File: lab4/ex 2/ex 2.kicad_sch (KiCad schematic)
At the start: 10 parts, among them J1 Conn_01x02_Male, U1 NE555D

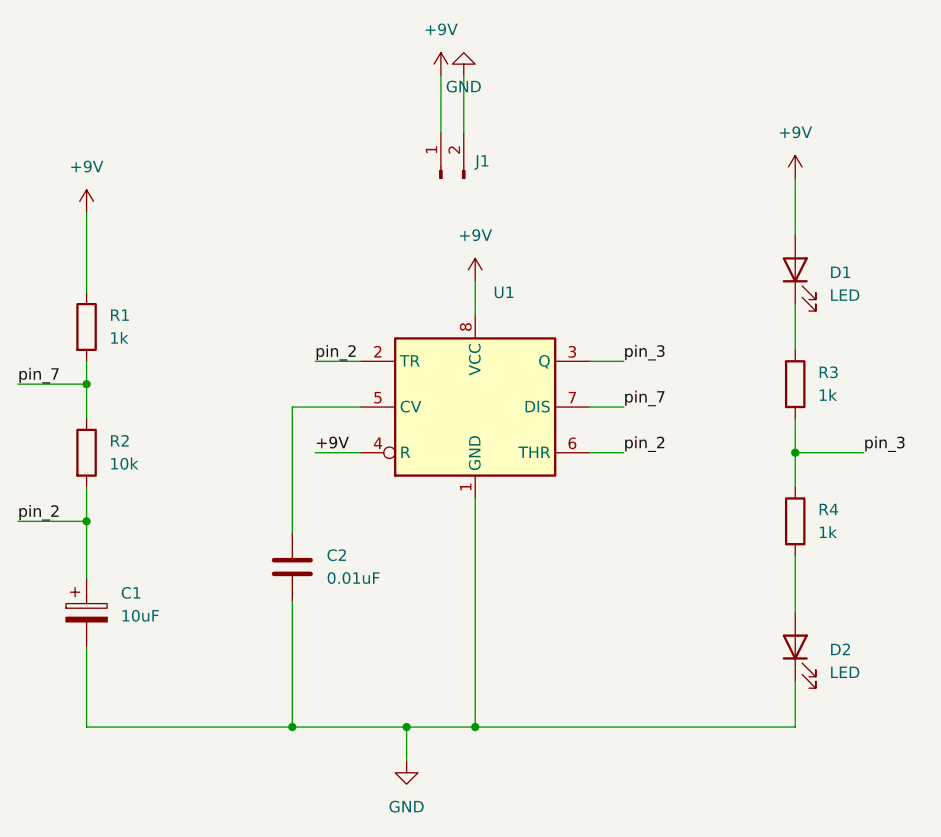
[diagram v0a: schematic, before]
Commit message: Updated schematics to include footprints and created a pcb layout
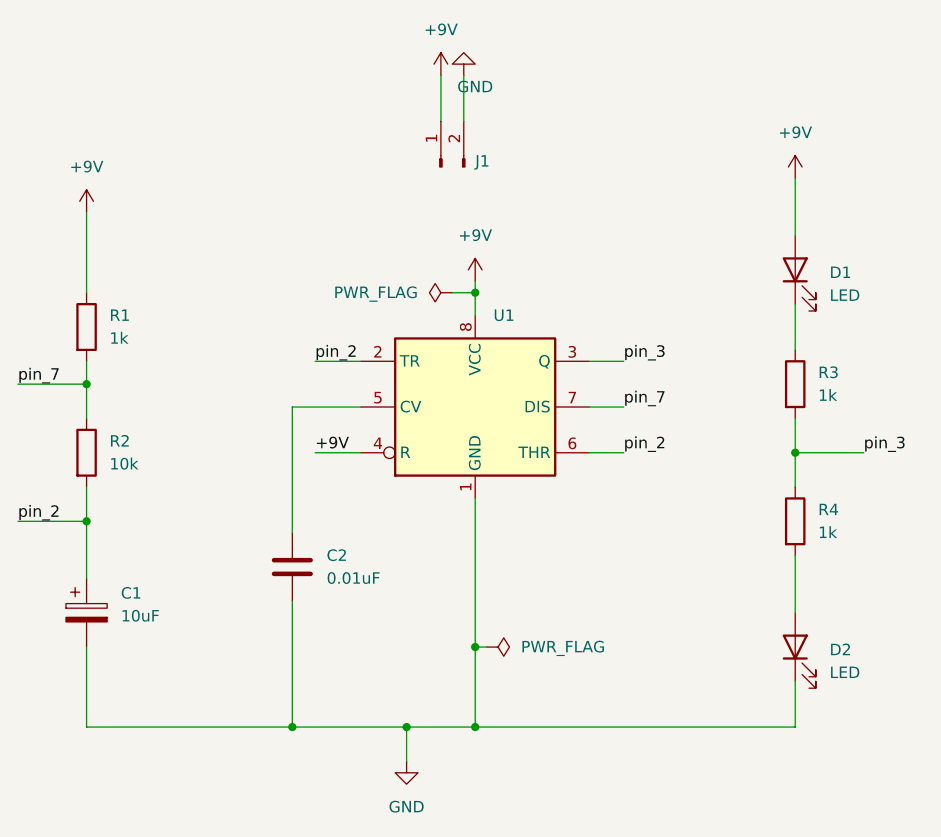
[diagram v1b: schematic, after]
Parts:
- C1: footprint (none) -> Capacitor_Tantalum_SMD:CP_EIA-3216-18_Kemet-A_Pad1.58x1.35mm_HandSolder
- C2: footprint (none) -> Capacitor_SMD:C_0805_2012Metric_Pad1.18x1.45mm_HandSolder
- D1, D2: footprint (none) -> LED_SMD:LED_1206_3216Metric_Pad1.42x1.75mm_HandSolder
- J1: footprint (none) -> TerminalBlock:TerminalBlock_bornier-2_P5.08mm
- R1, R2, R3, R4: footprint (none) -> Resistor_SMD:R_0805_2012Metric_Pad1.20x1.40mm_HandSolder
- U1: footprint Package_SO:SOIC-8_3.9x4.9mm_P1.27mm -> Package_SO:SOIC-8-1EP_3.9x4.9mm_P1.27mm_EP2.29x3mm
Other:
- moved on the sheet: J1
